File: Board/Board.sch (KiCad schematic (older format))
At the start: 52 parts, among them J1 Screw_Terminal_1x02, P1 USB_B, P2 CONN_01X05, P3 CONN_01X06, SW1 SW_SPST, SW2 SW_SPST, U1 MCP23016, U2 LM1117-3.3, U3 MCP9808, U4 ESP-12E

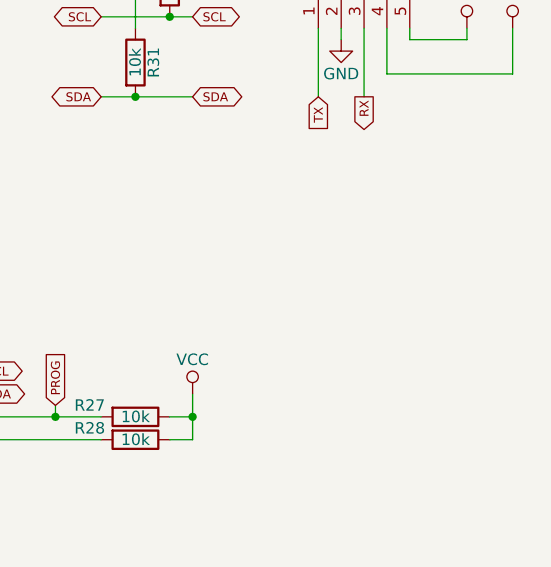
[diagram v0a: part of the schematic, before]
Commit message: I2C connector and more thermal decoupling
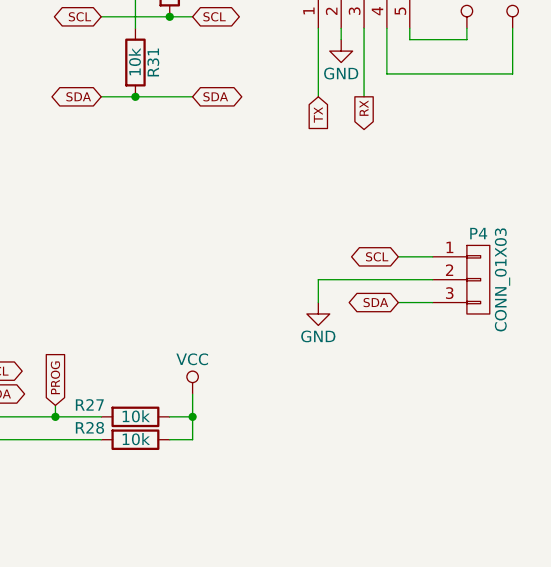
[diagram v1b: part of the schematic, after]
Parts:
- added P4: CONN_01X03, Pin_Headers:Pin_Header_Straight_1x03, symbol CONN_01X03
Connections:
- net GND: now also P4.2 (P2)
- net SCL: now also P4.1 (P1)
- net SDA: now also P4.3 (P3)
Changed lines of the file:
@@
 Wire Wire Line
 	8100 2900 8250 2900
+$Comp
+L CONN_01X03 P4
+U 1 1 5B82EAAC
+P 10450 2400
+F 0 "P4" H 10450 2600 50  0000 C CNN
+F 1 "CONN_01X03" V 10550 2400 50  0000 C CNN
+F 2 "Pin_Headers:Pin_Header_Straight_1x03" H 10450 2400 50  0001 C CNN
+F 3 "" H 10450 2400 50  0000 C CNN
+	1    10450 2400
+	1    0    0    -1
+$EndComp
+Text GLabel 10100 2300 0    39   BiDi ~ 0
+SCL
+Text GLabel 10100 2500 0    39   BiDi ~ 0
+SDA
+$Comp
+L GND #PWR033
+U 1 1 5B82F09B
+P 9750 2500
+F 0 "#PWR033" H 9750 2250 50  0001 C CNN
+F 1 "GND" H 9750 2350 50  0000 C CNN
+F 2 "" H 9750 2500 50  0000 C CNN
+F 3 "" H 9750 2500 50  0000 C CNN
+	1    9750 2500
+	1    0    0    -1
+$EndComp
+Wire Wire Line
+	10250 2300 10100 2300
+Wire Wire Line
+	10250 2500 10100 2500
+Wire Wire Line
+	10250 2400 9750 2400
+Wire Wire Line
+	9750 2400 9750 2500
 $EndSCHEMATC

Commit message: Minor changes for rev3
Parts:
- added R33: 0, Resistors_SMD:R_0603_HandSoldering, symbol R
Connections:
- net GND: now also R33.1
- net at P1.5 (shield): now also R33.2
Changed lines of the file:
@@
 $EndComp
 $Comp
-L VCC #PWR01
+L VCC #PWR17
 U 1 1 5AD1E3D6
 P 4950 2400
-F 0 "#PWR01" H 4950 2250 50  0001 C CNN
+F 0 "#PWR17" H 4950 2250 50  0001 C CNN
 F 1 "VCC" H 4950 2550 50  0000 C CNN
 F 2 "" H 4950 2400 50  0000 C CNN
@@
 $EndComp
 $Comp
-L GND #PWR02
+L GND #PWR26
 U 1 1 5AD1E3E7
 P 8150 3400
-F 0 "#PWR02" H 8150 3150 50  0001 C CNN
+F 0 "#PWR26" H 8150 3150 50  0001 C CNN
 F 1 "GND" H 8150 3250 50  0000 C CNN
 F 2 "" H 8150 3400 50  0000 C CNN
@@
 $EndComp
 $Comp
-L VCC #PWR03
+L VCC #PWR21
 U 1 1 5AD1E585
 P 6150 6000
-F 0 "#PWR03" H 6150 5850 50  0001 C CNN
+F 0 "#PWR21" H 6150 5850 50  0001 C CNN
 F 1 "VCC" H 6150 6150 50  0000 C CNN
 F 2 "" H 6150 6000 50  0000 C CNN
@@
 $EndComp
 $Comp
-L GND #PWR04
+L GND #PWR22
 U 1 1 5AD1E599
 P 6150 7250
-F 0 "#PWR04" H 6150 7000 50  0001 C CNN
+F 0 "#PWR22" H 6150 7000 50  0001 C CNN
 F 1 "GND" H 6150 7100 50  0000 C CNN
 F 2 "" H 6150 7250 50  0000 C CNN
@@
 $EndComp
 $Comp
-L GND #PWR05
+L GND #PWR30
 U 1 1 5AD1E8CC
 P 9850 1350
-F 0 "#PWR05" H 9850 1100 50  0001 C CNN
+F 0 "#PWR30" H 9850 1100 50  0001 C CNN
 F 1 "GND" H 9850 1200 50  0000 C CNN
 F 2 "" H 9850 1350 50  0000 C CNN
@@
 $EndComp
 $Comp
-L VCC #PWR06
+L VCC #PWR34
 U 1 1 5AD1E910
 P 10600 1300
-F 0 "#PWR06" H 10600 1150 50  0001 C CNN
+F 0 "#PWR34" H 10600 1150 50  0001 C CNN
 F 1 "VCC" H 10600 1450 50  0000 C CNN
 F 2 "" H 10600 1300 50  0000 C CNN
@@
 $EndComp
 $Comp
-L VDD #PWR07
+L VDD #PWR33
 U 1 1 5AD1E925
 P 10400 1300
-F 0 "#PWR07" H 10400 1150 50  0001 C CNN
+F 0 "#PWR33" H 10400 1150 50  0001 C CNN
 F 1 "VDD" H 10400 1450 50  0000 C CNN
 F 2 "" H 10400 1300 50  0000 C CNN
@@
 Alert
 $Comp
-L VCC #PWR08
+L VCC #PWR4
 U 1 1 5AD21696
 P 1150 7450
-F 0 "#PWR08" H 1150 7300 50  0001 C CNN
+F 0 "#PWR4" H 1150 7300 50  0001 C CNN
 F 1 "VCC" H 1150 7600 50  0000 C CNN
 F 2 "" H 1150 7450 50  0000 C CNN
@@
 SDA
 $Comp
-L VCC #PWR09
+L VCC #PWR27
 U 1 1 5AD3D501
 P 8950 800
-F 0 "#PWR09" H 8950 650 50  0001 C CNN
+F 0 "#PWR27" H 8950 650 50  0001 C CNN
 F 1 "VCC" H 8950 950 50  0000 C CNN
 F 2 "" H 8950 800 50  0000 C CNN
@@
 $EndComp
 $Comp
-L GND #PWR010
+L GND #PWR10
 U 1 1 5AD3FEC4
 P 1650 2300
-F 0 "#PWR010" H 1650 2050 50  0001 C CNN
+F 0 "#PWR10" H 1650 2050 50  0001 C CNN
 F 1 "GND" H 1650 2150 50  0000 C CNN
 F 2 "" H 1650 2300 50  0000 C CNN
@@
 	1650 1900 1650 1800
 $Comp
-L GND #PWR011
+L GND #PWR8
 U 1 1 5AD40223
 P 1650 1300
-F 0 "#PWR011" H 1650 1050 50  0001 C CNN
+F 0 "#PWR8" H 1650 1050 50  0001 C CNN
 F 1 "GND" H 1650 1150 50  0000 C CNN
 F 2 "" H 1650 1300 50  0000 C CNN
@@
 	1650 1200 1650 1300
 $Comp
-L VDD #PWR012
+L VDD #PWR7
 U 1 1 5AD40ECC
 P 1650 900
-F 0 "#PWR012" H 1650 750 50  0001 C CNN
+F 0 "#PWR7" H 1650 750 50  0001 C CNN
 F 1 "VDD" H 1650 1050 50  0000 C CNN
 F 2 "" H 1650 900 50  0000 C CNN
@@
 $EndComp
 $Comp
-L VDD #PWR013
+L VDD #PWR9
 U 1 1 5AD411EA
 P 1650 1800
-F 0 "#PWR013" H 1650 1650 50  0001 C CNN
+F 0 "#PWR9" H 1650 1650 50  0001 C CNN
 F 1 "VDD" H 1650 1950 50  0000 C CNN
 F 2 "" H 1650 1800 50  0000 C CNN
@@
 $EndComp
 $Comp
-L VDD #PWR014
+L VDD #PWR14
 U 1 1 5AD4147C
 P 2550 900
-F 0 "#PWR014" H 2550 750 50  0001 C CNN
+F 0 "#PWR14" H 2550 750 50  0001 C CNN
 F 1 "VDD" H 2550 1050 50  0000 C CNN
 F 2 "" H 2550 900 50  0000 C CNN
@@
 $EndComp
 $Comp
-L GND #PWR015
+L GND #PWR15
 U 1 1 5AD414E4
 P 2550 1900
-F 0 "#PWR015" H 2550 1650 50  0001 C CNN
+F 0 "#PWR15" H 2550 1650 50  0001 C CNN
 F 1 "GND" H 2550 1750 50  0000 C CNN
 F 2 "" H 2550 1900 50  0000 C CNN
@@
 	3050 1800 3050 1300
 $Comp
-L VCC #PWR016
+L VCC #PWR16
 U 1 1 5AD41DB7
 P 3850 900
-F 0 "#PWR016" H 3850 750 50  0001 C CNN
+F 0 "#PWR16" H 3850 750 50  0001 C CNN
 F 1 "VCC" H 3850 1050 50  0000 C CNN
 F 2 "" H 3850 900 50  0000 C CNN
@@
 Connection ~ 8600 3000
 $Comp
-L VCC #PWR017
+L VCC #PWR28
 U 1 1 5AD4B964
 P 9200 2900
-F 0 "#PWR017" H 9200 2750 50  0001 C CNN
+F 0 "#PWR28" H 9200 2750 50  0001 C CNN
 F 1 "VCC" H 9200 3050 50  0000 C CNN
 F 2 "" H 9200 2900 50  0000 C CNN
@@
 $EndComp
 $Comp
-L GND #PWR018
+L GND #PWR13
 U 1 1 5AD38C7F
 P 2350 5700
-F 0 "#PWR018" H 2350 5450 50  0001 C CNN
+F 0 "#PWR13" H 2350 5450 50  0001 C CNN
 F 1 "GND" H 2350 5550 50  0000 C CNN
 F 2 "" H 2350 5700 50  0000 C CNN
@@
 Connection ~ 2350 5600
 $Comp
-L GND #PWR019
+L GND #PWR11
 U 1 1 5AD392B5
 P 1700 5400
-F 0 "#PWR019" H 1700 5150 50  0001 C CNN
+F 0 "#PWR11" H 1700 5150 50  0001 C CNN
 F 1 "GND" H 1700 5250 50  0000 C CNN
 F 2 "" H 1700 5400 50  0000 C CNN
@@
 Connection ~ 1400 3700
 $Comp
-L GND #PWR020
+L GND #PWR6
 U 1 1 5AD3A94D
 P 1400 4200
-F 0 "#PWR020" H 1400 3950 50  0001 C CNN
+F 0 "#PWR6" H 1400 3950 50  0001 C CNN
 F 1 "GND" H 1400 4050 50  0000 C CNN
 F 2 "" H 1400 4200 50  0000 C CNN
@@
 	1850 4200 1800 4200
 $Comp
-L VCC #PWR021
+L VCC #PWR5
 U 1 1 5AD3B1E1
 P 1400 3250
-F 0 "#PWR021" H 1400 3100 50  0001 C CNN
+F 0 "#PWR5" H 1400 3100 50  0001 C CNN
 F 1 "VCC" H 1400 3400 50  0000 C CNN
 F 2 "" H 1400 3250 50  0000 C CNN
@@
 	1400 3250 1400 3350
 $Comp
-L VCC #PWR022
+L VCC #PWR12
 U 1 1 5AD3B513
 P 2350 3250
-F 0 "#PWR022" H 2350 3100 50  0001 C CNN
+F 0 "#PWR12" H 2350 3100 50  0001 C CNN
 F 1 "VCC" H 2350 3400 50  0000 C CNN
 F 2 "" H 2350 3250 50  0000 C CNN
@@
 	2350 3250 2350 3500
 $Comp
-L VCC #PWR023
+L VCC #PWR2
 U 1 1 5AD3BA06
 P 1150 4700
-F 0 "#PWR023" H 1150 4550 50  0001 C CNN
+F 0 "#PWR2" H 1150 4550 50  0001 C CNN
 F 1 "VCC" H 1150 4850 50  0000 C CNN
 F 2 "" H 1150 4700 50  0000 C CNN
@@
 $EndComp
 $Comp
-L GND #PWR024
+L GND #PWR3
 U 1 1 5AD3BB78
 P 1150 5200
-F 0 "#PWR024" H 1150 4950 50  0001 C CNN
+F 0 "#PWR3" H 1150 4950 50  0001 C CNN
 F 1 "GND" H 1150 5050 50  0000 C CNN
 F 2 "" H 1150 5200 50  0000 C CNN
@@
 	5200 4450 5200 4950
 $Comp
-L VCC #PWR025
+L VCC #PWR23
 U 1 1 5AD4F68E
 P 6200 4200
-F 0 "#PWR025" H 6200 4050 50  0001 C CNN
+F 0 "#PWR23" H 6200 4050 50  0001 C CNN
 F 1 "VCC" H 6200 4350 50  0000 C CNN
 F 2 "" H 6200 4200 50  0000 C CNN
@@
 	4950 5100 5200 5100
 $Comp
-L GND #PWR026
+L GND #PWR18
 U 1 1 5AD4FEAF
 P 4950 5200
-F 0 "#PWR026" H 4950 4950 50  0001 C CNN
+F 0 "#PWR18" H 4950 4950 50  0001 C CNN
 F 1 "GND" H 4950 5050 50  0000 C CNN
 F 2 "" H 4950 5200 50  0000 C CNN
@@
 $EndComp
 $Comp
-L GND #PWR027
+L GND #PWR25
 U 1 1 5AD51CC2
 P 7500 1700
-F 0 "#PWR027" H 7500 1450 50  0001 C CNN
+F 0 "#PWR25" H 7500 1450 50  0001 C CNN
 F 1 "GND" H 7500 1550 50  0000 C CNN
 F 2 "" H 7500 1700 50  0000 C CNN
@@
 	5600 1000 5700 1000
 $Comp
-L GND #PWR028
+L GND #PWR19
 U 1 1 5AD69753
 P 5050 1100
-F 0 "#PWR028" H 5050 850 50  0001 C CNN
+F 0 "#PWR19" H 5050 850 50  0001 C CNN
 F 1 "GND" H 5050 950 50  0000 C CNN
 F 2 "" H 5050 1100 50  0000 C CNN
@@
 	5600 1400 5700 1400
 $Comp
-L GND #PWR029
+L GND #PWR20
 U 1 1 5AD69C58
 P 5050 1500
-F 0 "#PWR029" H 5050 1250 50  0001 C CNN
+F 0 "#PWR20" H 5050 1250 50  0001 C CNN
 F 1 "GND" H 5050 1350 50  0000 C CNN
 F 2 "" H 5050 1500 50  0000 C CNN
@@
 	7500 1550 7500 1700
 $Comp
-L VCC #PWR030
+L VCC #PWR24
 U 1 1 5AD7B5BE
 P 7500 1050
-F 0 "#PWR030" H 7500 900 50  0001 C CNN
+F 0 "#PWR24" H 7500 900 50  0001 C CNN
 F 1 "VCC" H 7500 1200 50  0000 C CNN
 F 2 "" H 7500 1050 50  0000 C CNN
@@
 	5050 2600 4950 2600
 $Comp
-L GND #PWR031
+L GND #PWR32
 U 1 1 5AD82799
 P 10050 5400
-F 0 "#PWR031" H 10050 5150 50  0001 C CNN
+F 0 "#PWR32" H 10050 5150 50  0001 C CNN
 F 1 "GND" H 10050 5250 50  0000 C CNN
 F 2 "" H 10050 5400 50  0000 C CNN
@@
 $EndComp
 $Comp
-L VCC #PWR032
+L VCC #PWR31
 U 1 1 5AD8279F
 P 10050 4700
-F 0 "#PWR032" H 10050 4550 50  0001 C CNN
+F 0 "#PWR31" H 10050 4550 50  0001 C CNN
 F 1 "VCC" H 10050 4850 50  0000 C CNN
 F 2 "" H 10050 4700 50  0000 C CNN
@@
 SDA
 $Comp
-L GND #PWR033
+L GND #PWR29
 U 1 1 5B82F09B
 P 9750 2500
-F 0 "#PWR033" H 9750 2250 50  0001 C CNN
+F 0 "#PWR29" H 9750 2250 50  0001 C CNN
 F 1 "GND" H 9750 2350 50  0000 C CNN
 F 2 "" H 9750 2500 50  0000 C CNN
@@
 Wire Wire Line
 	9750 2400 9750 2500
+$Comp
+L R R33
+U 1 1 5BA92E19
+P 1100 2600
+F 0 "R33" V 1000 2600 50  0000 C CNN
+F 1 "0" V 1100 2600 50  0000 C CNN
+F 2 "Resistors_SMD:R_0603_HandSoldering" V 1030 2600 50  0001 C CNN
+F 3 "" H 1100 2600 50  0000 C CNN
+	1    1100 2600
+	-1   0    0    1
+$EndComp
+$Comp
+L GND #PWR1
+U 1 1 5BA92F35
+P 1100 2800
+F 0 "#PWR1" H 1100 2550 50  0001 C CNN
+F 1 "GND" H 1100 2650 50  0000 C CNN
+F 2 "" H 1100 2800 50  0000 C CNN
+F 3 "" H 1100 2800 50  0000 C CNN
+	1    1100 2800
+	1    0    0    -1
+$EndComp
+Wire Wire Line
+	1100 2400 1100 2450
+Wire Wire Line
+	1100 2750 1100 2800
 $EndSCHEMATC
